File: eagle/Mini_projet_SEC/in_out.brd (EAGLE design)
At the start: 100 x 80 mm, 66 parts, among them Q1 MOSFET-NCHANNELAO3404A, Q10 MOSFET-NCHANNELAO3404A, Q11 MOSFET-NCHANNELAO3404A, Q12 MOSFET-NCHANNELAO3404A, Q2 MOSFET-NCHANNELAO3404A, Q3 MOSFET-NCHANNELAO3404A, Q4 MOSFET-NCHANNELAO3404A, Q5 MOSFET-NCHANNELAO3404A, Q6 MOSFET-NCHANNELAO3404A, Q7 MOSFET-NCHANNELAO3404A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

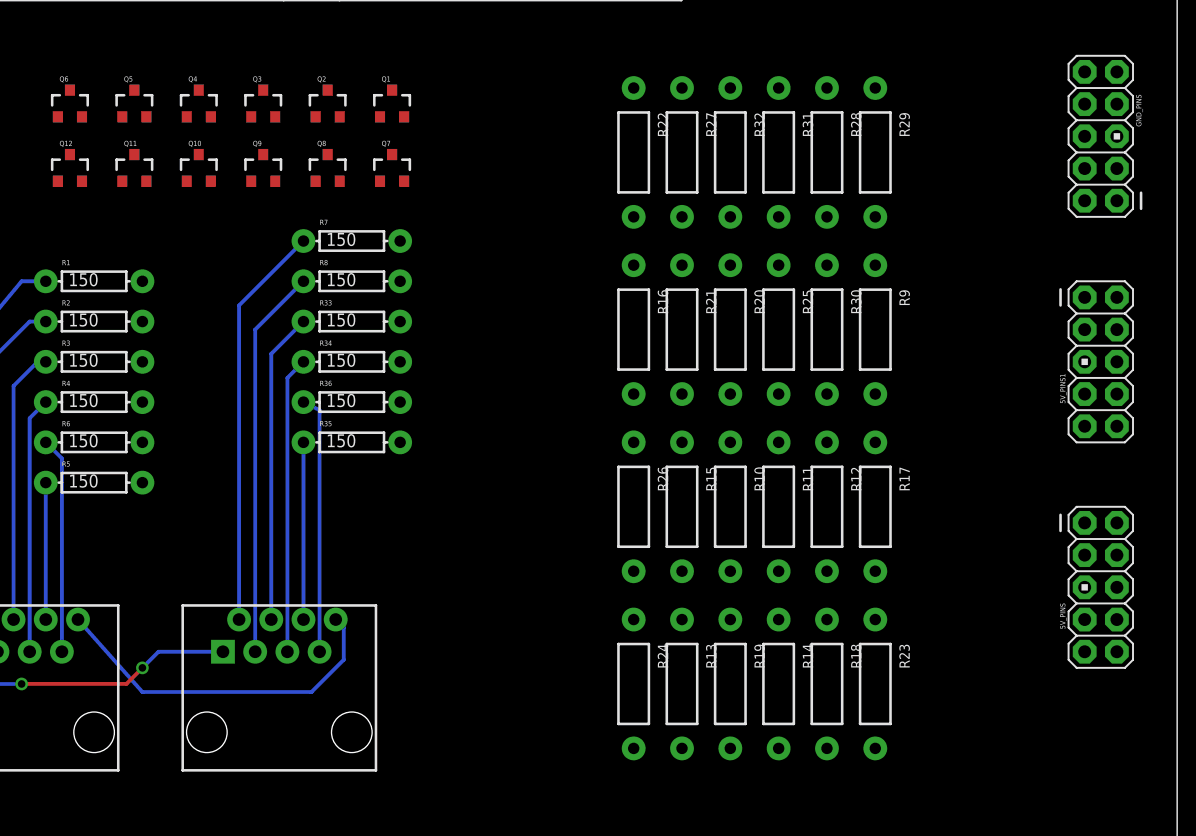
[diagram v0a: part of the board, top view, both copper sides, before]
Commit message: First implementation of Simon game with DMX + keyboard.
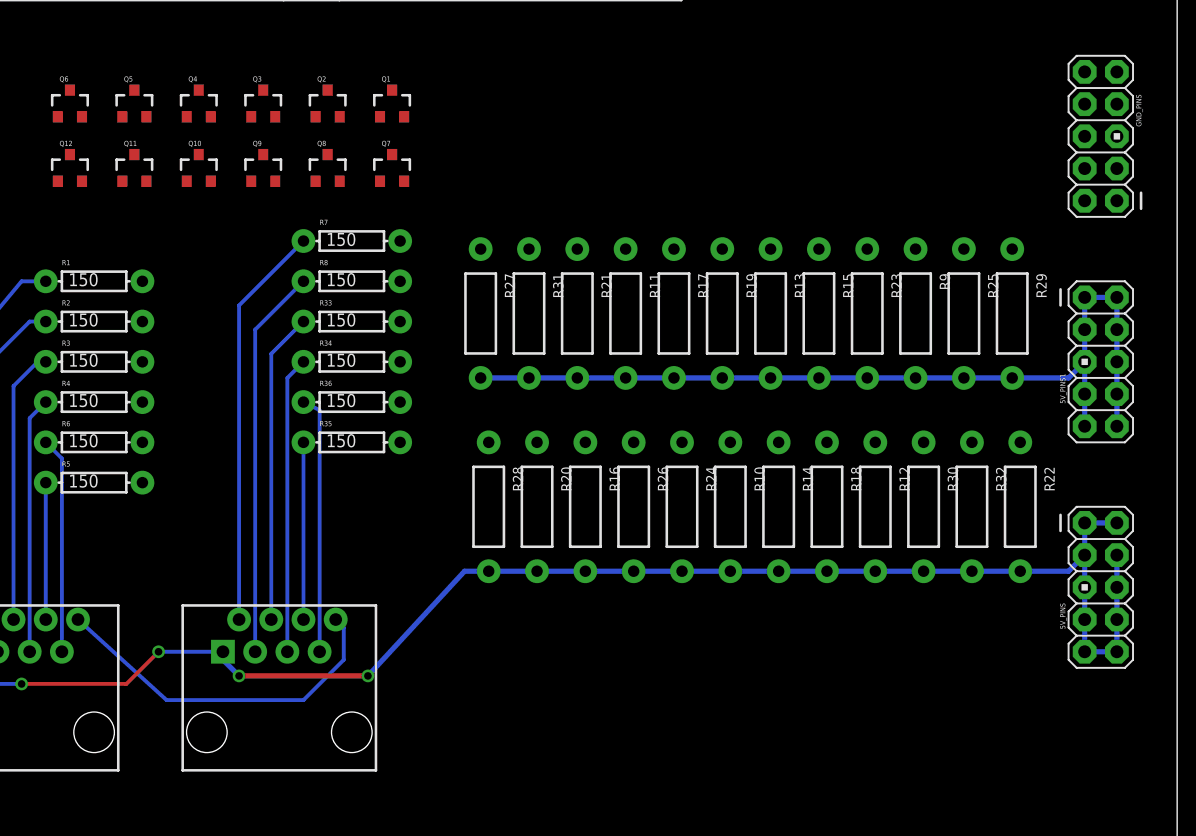
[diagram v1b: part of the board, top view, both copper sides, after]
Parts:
- moved R22 41.3 mm to (87.6, 29.2)
- moved R28 38.6 mm to (45.7, 29.2)
- moved R32 33.8 mm to (83.8, 29.2)
- moved R13 30.0 mm to (67.9, 44.5)
- moved R19 29.2 mm to (64.1, 44.5)
- moved R23 29.2 mm to (75.6, 44.5)
- moved R31 23.4 mm to (48.9, 44.5)
- moved R17 22.0 mm to (60.3, 44.5)
- moved R20 20.7 mm to (49.5, 29.2)
- moved R27 20.3 mm to (45.1, 44.5)
- moved R11 19.4 mm to (56.5, 44.5)
- moved R15 18.7 mm to (71.8, 44.5)
- moved R29 16.7 mm to (87.0, 44.5)
- moved R30 15.9 mm to (80.0, 29.2)
- moved R25 14.7 mm to (83.2, 44.5)
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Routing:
- net 5V: track 23.5 -> 119.6 mm, vias 2 -> 4
- net 3.3V: track 0.00 -> 71.0 mm
